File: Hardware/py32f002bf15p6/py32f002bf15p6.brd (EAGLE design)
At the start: 43.9 x 18.6 mm, 26 parts, among them IC1 PY32F002BF15P6TU, IC2 AP2114HA-3.3TRG1, J1 USB_MINI-B_SMT, Y1 DSC6083CI1A-350K000T

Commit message: Generate final gerbers and rename directories to match chip name
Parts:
- removed R2: (no value), rcl:R0805
- removed S2: RESET, SparkFun-Switches:TACTILE_SWITCH_SMD_6.0X3.5MM
- added R5: (no value), rcl:R0805
- added S3: RESET, SparkFun-Switches:TACTILE_SWITCH_SMD_6.0X3.5MM
- moved C1 0.64 mm to (17.4, 4.95)
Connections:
- net U1RX renamed TXD
- net U1TX renamed RXD
- removed net PA3: IC1.19, J3.2, JP2.2
- removed net PA4: IC1.20, J3.1, JP1.2
- new net PA3-UTX: IC1.19, J3.2, JP1.2
- new net PA4-URX: IC1.20, J3.1, JP2.2
- net +3V3: now also S3.2; no longer R2.2
- net GND: now also R5.1; no longer S2.1
- net N$1: now also R5.2, S3.1; no longer R2.1, S2.2
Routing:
- net PA3: track 20.3 -> 0.00 mm, vias 2 -> 0
- net PA4-URX: track 0.00 -> 19.1 mm
- net PA4: track 18.1 -> 0.00 mm
- net PA3-UTX: track 0.00 -> 16.0 mm
- net N$1: track 15.8 -> 27.4 mm
- net +3V3: track 95.3 -> 99.1 mm, vias 3 -> 4
- net GND: track 129.5 -> 131.0 mm, vias 16 -> 15
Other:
- board text added: "PYBUG32-2b RevC"
- board text removed: "JP1 - PA4/USB_RX JP2 - PA3/USB_TX JP3 - PA0/BTN JP4 - PA1/LED"
- board text removed: "PYBUG32-2b RevA"

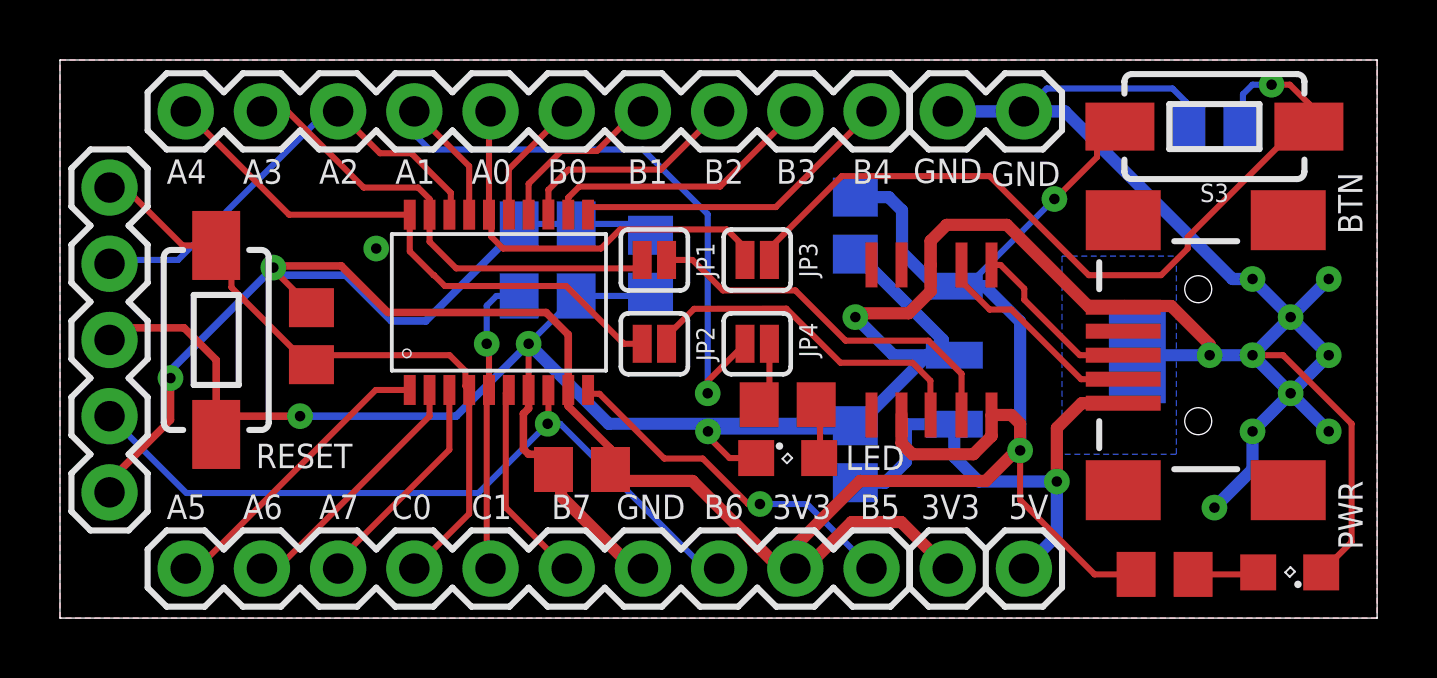
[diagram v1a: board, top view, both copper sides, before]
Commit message: Replaced 4.7uf 0805 caps for larger 1206 parts
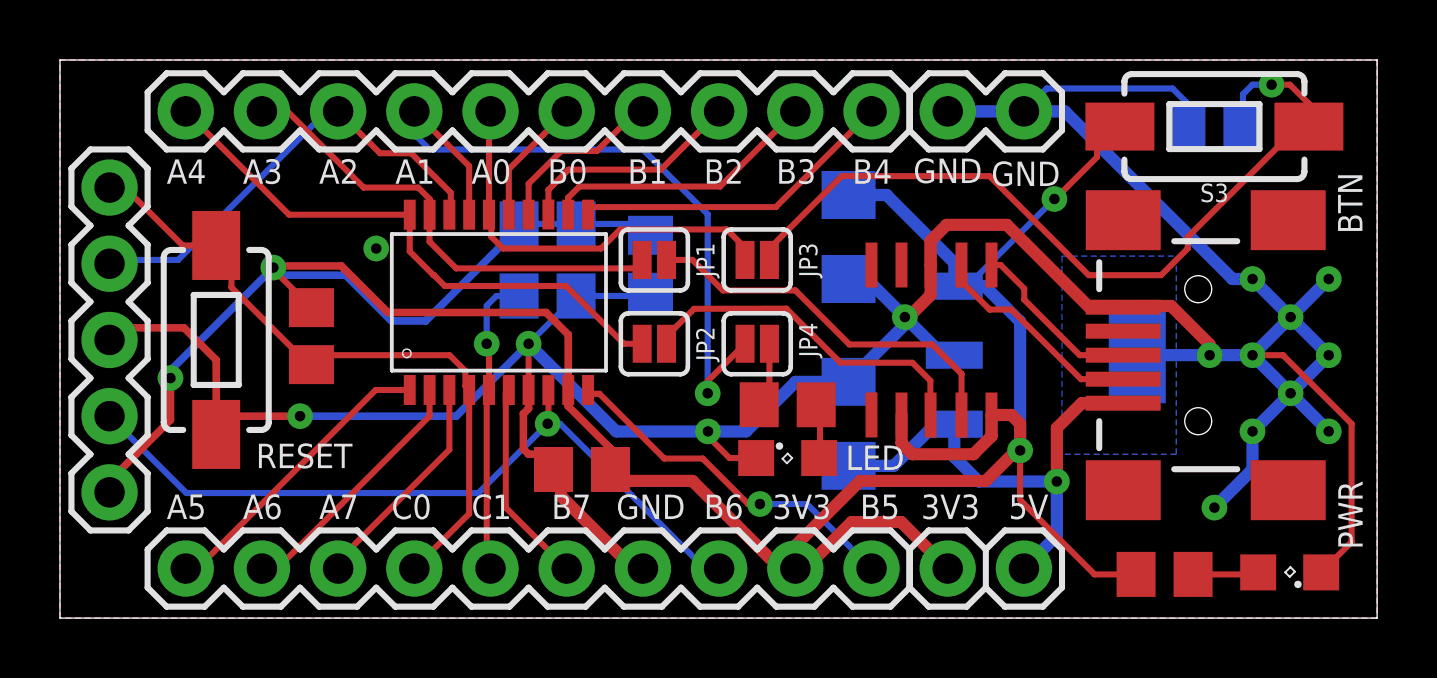
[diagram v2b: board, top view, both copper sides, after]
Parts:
- C10, C9: device rcl:C0805 -> rcl:C1206
- moved C10 1.04 mm to (26.3, 6.47)
- moved C9 0.44 mm to (26.3, 12.7)
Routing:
- net GND: track 131.0 -> 119.5 mm
- net VBUS: track 17.4 -> 16.6 mm
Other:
- board text added: "PYBUG32-2b RevD"
- board text removed: "PYBUG32-2b RevC"

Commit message: Updated silkscreen, removed reset header pin
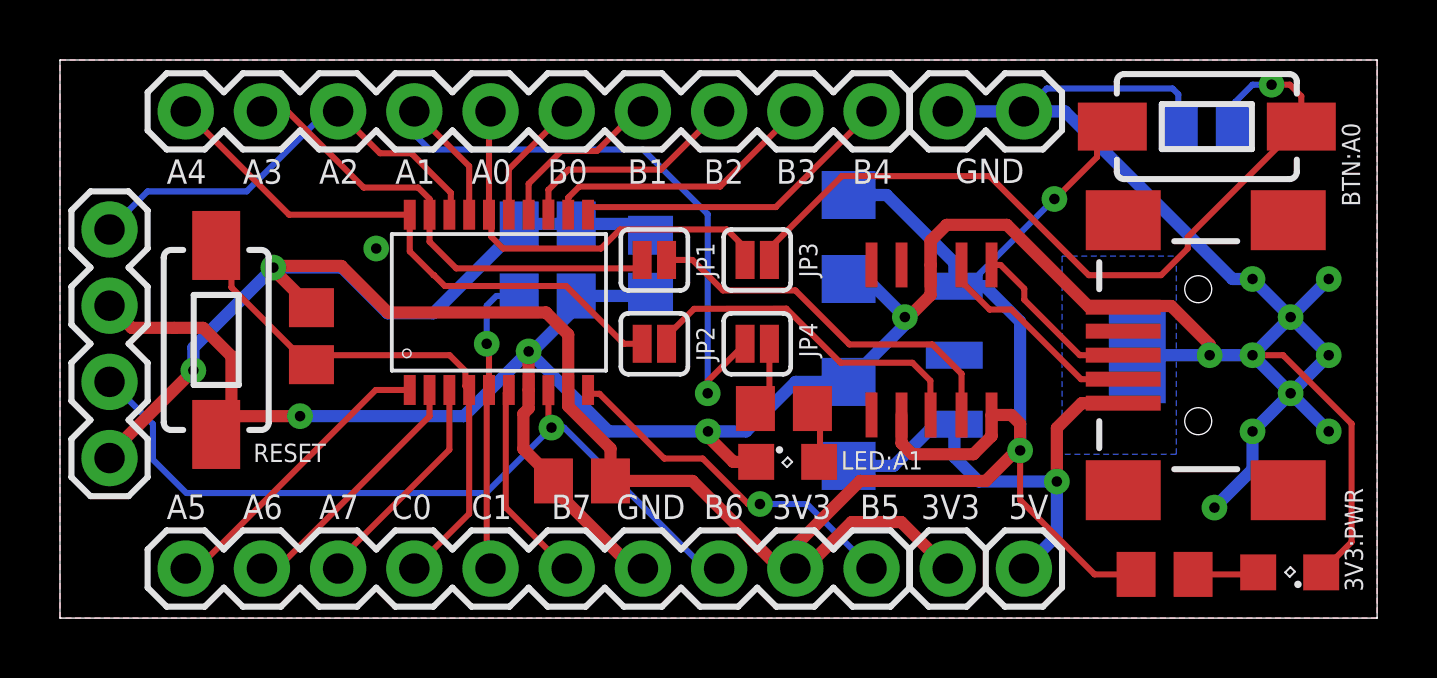
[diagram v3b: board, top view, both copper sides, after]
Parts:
- removed J2: (no value), SparkFun-Connectors:1X05
- added J7: (no value), SparkFun-Connectors:1X04
- moved C1 0.38 mm to (17.4, 4.57)
- moved R5 0.25 mm to (38.2, 16.4)
- moved S3 0.25 mm to (38.2, 16.4)
- moved R3 0.18 mm to (24.1, 6.99)
- moved LED 0.13 mm to (24.3, 5.21)
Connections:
- net +3V3: now also J7.4; no longer J2.5
- net GND: now also J7.2; no longer J2.3
- net PA2-SWC: now also J7.1; no longer J2.2
- net PB6-SWD: now also J7.3; no longer J2.4
- net PC0-RST: no longer J2.1
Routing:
- net PC0-RST: track 22.6 -> 18.2 mm
- net GND: track 119.5 -> 117.5 mm
- net +3V3: track 99.0 -> 97.8 mm
- net PB6-SWD: track 25.5 -> 26.7 mm
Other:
- board text added: "3V3:PWR"
- board text added: "BTN:A0"
- board text added: "LED:A1"
- board text added: "RX:A4"
- board text added: "SWC: A2"
- board text added: "SWD: B6"
- board text added: "TX:A3"
- board text removed: "BTN"
- board text removed: "RST"
